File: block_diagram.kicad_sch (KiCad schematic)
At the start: 0 parts

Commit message: Major Changes - Schematic Done??
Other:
- sheet STM32G491RET6 renamed STM32G4
- removed sheet Duplicate Sensors
- sheet Analog ports: added I2S2_CK, I2S2_SD, I2S2_WS, LEFT_SD_MODE, RIGHT_SD_MODE; removed DAC_LEFT_SD_MODE, DAC_RIGHT_SD_MODE, I2S3_CK, I2S3_SD, I2S3_WS
- sheet ESP32C3 ports: added SPI1_MISO, SPI1_MOSI, SPI1_SCLK, SPI_CS_ESP; removed none
- sheet Peripherials ports: added none; removed VBUS_ESP
- sheet Power ports: added 5V_VOLTS, I2C3_SCL, I2C3_SDA, MATRIX_PWR_EN; removed none
- sheet STM32G4 ports: added 5V_VOLTS, ALS_ADC, I2S2_CK, I2S2_SD, I2S2_WS, INT_TEMP_ALERT, LEFT_SD_MODE, MATRIX_PWR_EN, MIC, RIGHT_SD_MODE, SPI1_MISO, SPI1_MOSI, SPI1_SCLK, SPI_CS_ESP, STM32_USB_D_N, STM32_USB_D_P, TV_IR_PWM_1, TV_IR_PWM_2; removed ADC1_IN3, MIC_ADC, PA_3, PC_7
- sheet Sensors ports: added ALS_ADC, I2S3_CK, I2S3_SD, I2S3_WS, INT_TEMP_ALERT, TV_IR_PWM_1, TV_IR_PWM_2; removed LightSense, PA_3, PC_7

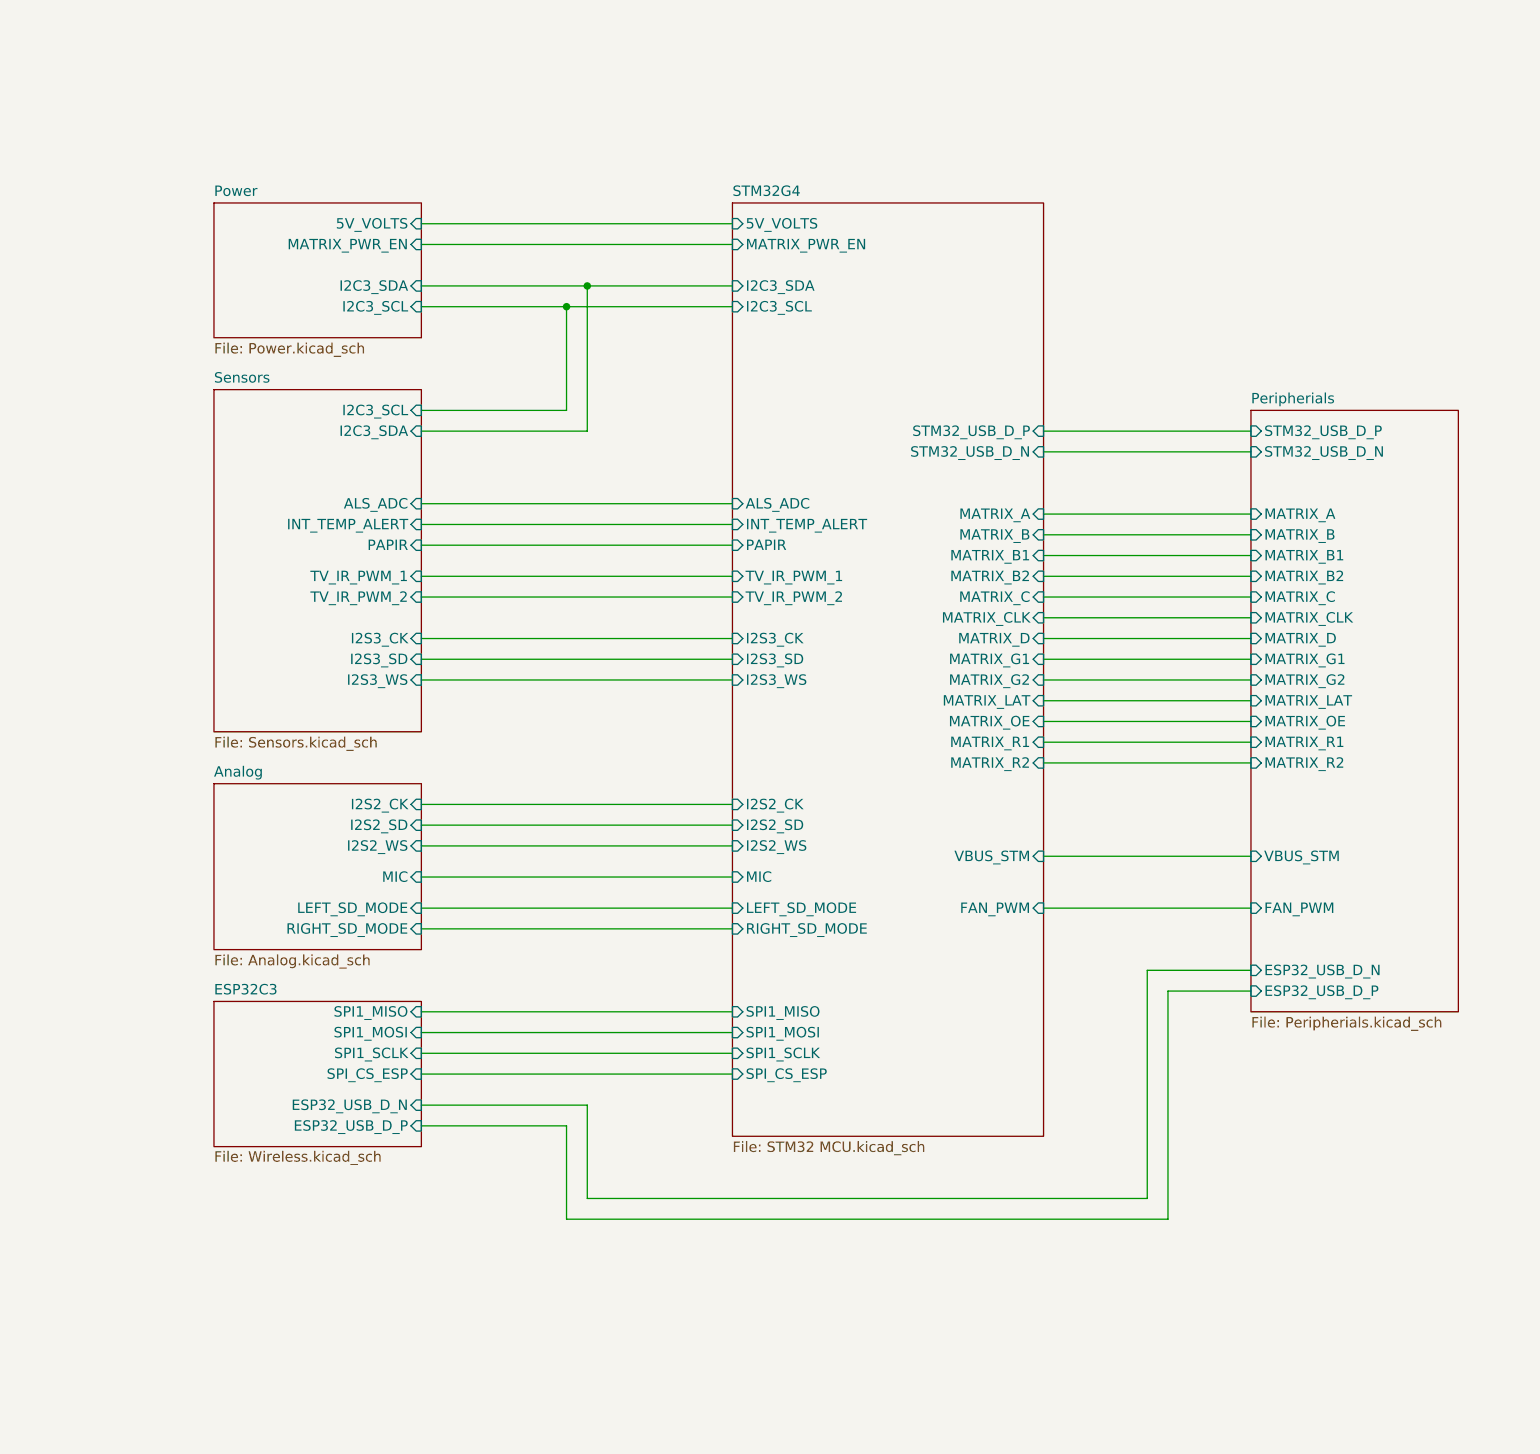
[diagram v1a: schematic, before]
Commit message: PCB Start, Schematic polish
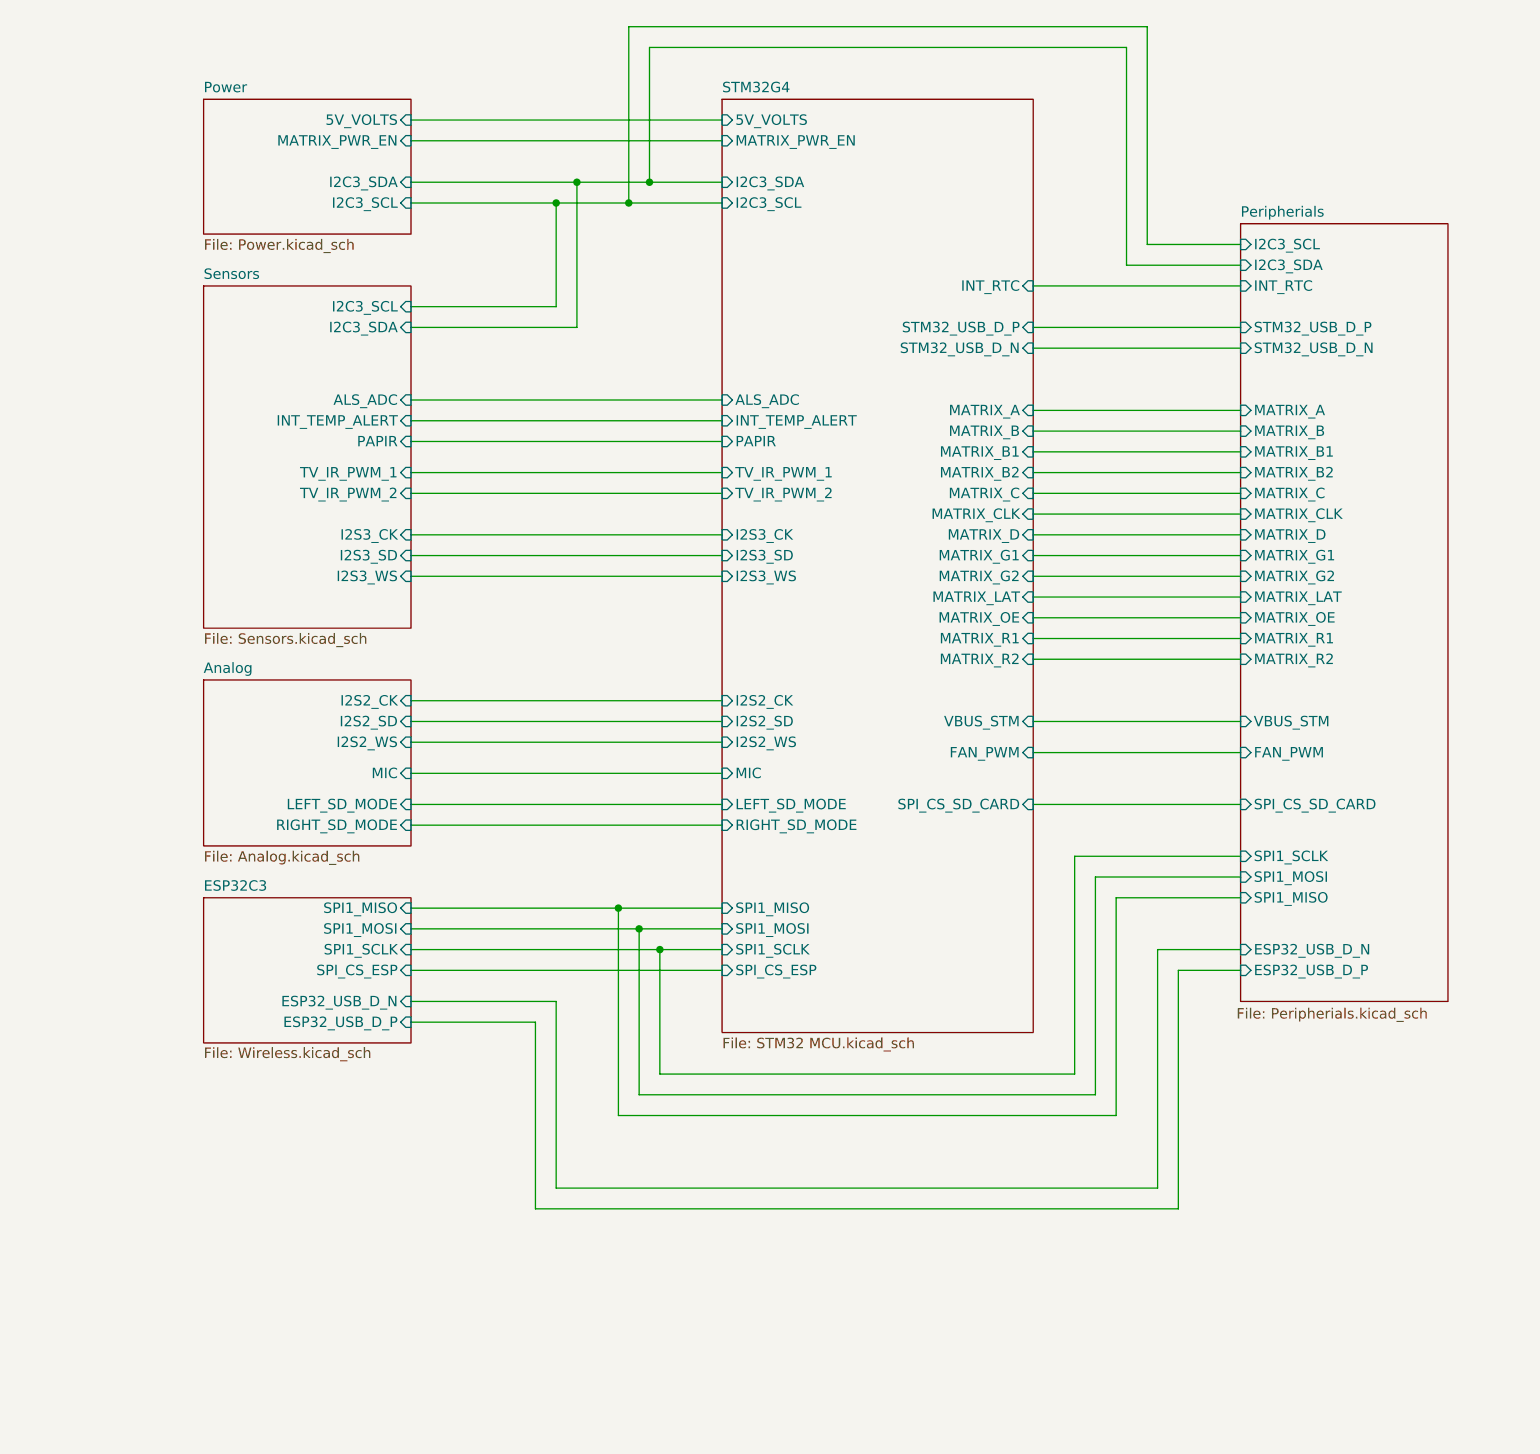
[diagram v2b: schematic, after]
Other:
- sheet Peripherials ports: added I2C3_SCL, I2C3_SDA, INT_RTC, SPI1_MISO, SPI1_MOSI, SPI1_SCLK, SPI_CS_SD_CARD; removed none
- sheet STM32G4 ports: added INT_RTC, SPI_CS_SD_CARD; removed none

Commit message: Minor PCB Changes
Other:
- sheet Peripherials ports: added USB-C_CC1, USB-C_CC2; removed none
- sheet STM32G4 ports: added USB-C_CC1, USB-C_CC2; removed none
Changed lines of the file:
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@@
+	(wire
+		(pts
+			(xy 163.83 40.64) (xy 189.23 40.64)
+		)
+		(stroke
+			(width 0)
+			(type default)
+		)
+	)
 	(wire
 		(pts
@@
 	(wire
 		(pts
-			(xy 177.8 43.18) (xy 177.8 16.51)
+			(xy 177.8 33.02) (xy 177.8 16.51)
 		)
 		(stroke
@@
 	(wire
 		(pts
-			(xy 189.23 43.18) (xy 177.8 43.18)
+			(xy 189.23 33.02) (xy 177.8 33.02)
 		)
 		(stroke
@@
 	(wire
 		(pts
-			(xy 175.26 45.72) (xy 175.26 19.05)
-		)
-		(stroke
-			(width 0)
-			(type default)
-		)
-	)
-	(wire
-		(pts
-			(xy 189.23 45.72) (xy 175.26 45.72)
+			(xy 175.26 35.56) (xy 175.26 19.05)
+		)
+		(stroke
+			(width 0)
+			(type default)
+		)
+	)
+	(wire
+		(pts
+			(xy 189.23 35.56) (xy 175.26 35.56)
 		)
 		(stroke
@@
 		(pts
 			(xy 163.83 66.04) (xy 189.23 66.04)
+		)
+		(stroke
+			(width 0)
+			(type default)
+		)
+	)
+	(wire
+		(pts
+			(xy 163.83 43.18) (xy 189.23 43.18)
 		)
 		(stroke
@@
 			)
 		)
+		(pin "USB-C_CC1" input
+			(at 163.83 40.64 0)
+			(effects
+				(font
+					(size 1.27 1.27)
+				)
+				(justify right)
+			)
+		)
+		(pin "USB-C_CC2" input
+			(at 163.83 43.18 0)
+			(effects
+				(font
+					(size 1.27 1.27)
+				)
+				(justify right)
+			)
+		)
 		(instances
 			(project "SeniorDesign_PCB"
@@
 	)
 	(sheet
-		(at 189.23 40.64)
-		(size 25.4 95.25)
+		(at 189.23 29.21)
+		(size 25.4 105.41)
 		(exclude_from_sim no)
 		(in_bom yes)
@@
 		)
 		(property "Sheetname" "Peripherials"
-			(at 189.23 39.9284 0)
+			(at 189.23 28.4984 0)
 			(show_name no)
 			(do_not_autoplace no)
@@
 		)
 		(property "Sheetfile" "Peripherials.kicad_sch"
-			(at 188.722 136.652 0)
+			(at 189.484 135.636 0)
 			(show_name no)
 			(do_not_autoplace no)
@@
 		)
 		(pin "I2C3_SCL" input
-			(at 189.23 43.18 180)
+			(at 189.23 33.02 180)
 			(effects
 				(font
@@
 		)
 		(pin "I2C3_SDA" input
-			(at 189.23 45.72 180)
+			(at 189.23 35.56 180)
 			(effects
 				(font
@@
 			(effects
 				(font
+					(size 1.27 1.27)
+				)
+				(justify left)
+			)
+		)
+		(pin "USB-C_CC1" input
+			(at 189.23 40.64 180)
+			(effects
+				(font
+					(size 1.27 1.27)
+				)
+				(justify left)
+			)
+		)
+		(pin "USB-C_CC2" input
+			(at 189.23 43.18 180)
+			(effects
+				(font

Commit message: Schematic tiddy up
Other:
- title: (none) -> Block Diagram Schematic
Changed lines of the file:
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@@
 	(generator_version "10.0")
 	(paper "A4")
+	(title_block
+		(title "Block Diagram Schematic")
+		(date "2026-10-17")
+		(rev "0")
+		(comment 1 "Javier Aldana + Xander Beal")
+	)
 	(junction
 		(at 116.84 35.56)

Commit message: Final PCB from Xander
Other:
- sheet Peripherials ports: added none; removed USB-C_CC1, USB-C_CC2
- sheet STM32G4 ports: added none; removed USB-C_CC1, USB-C_CC2
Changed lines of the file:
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@@
-	(wire
-		(pts
-			(xy 163.83 40.64) (xy 189.23 40.64)
-		)
-		(stroke
-			(width 0)
-			(type default)
-		)
-	)
 	(wire
 		(pts
@@
 		(pts
 			(xy 163.83 66.04) (xy 189.23 66.04)
-		)
-		(stroke
-			(width 0)
-			(type default)
-		)
-	)
-	(wire
-		(pts
-			(xy 163.83 43.18) (xy 189.23 43.18)
 		)
 		(stroke
@@
 			)
 		)
-		(pin "USB-C_CC1" input
-			(at 163.83 40.64 0)
-			(effects
-				(font
-					(size 1.27 1.27)
-				)
-				(justify right)
-			)
-		)
-		(pin "USB-C_CC2" input
-			(at 163.83 43.18 0)
-			(effects
-				(font
-					(size 1.27 1.27)
-				)
-				(justify right)
-			)
-		)
 		(instances
 			(project "SeniorDesign_PCB"
@@
 			(effects
 				(font
-					(size 1.27 1.27)
-				)
-				(justify left)
-			)
-		)
-		(pin "USB-C_CC1" input
-			(at 189.23 40.64 180)
-			(effects
-				(font
-					(size 1.27 1.27)
-				)
-				(justify left)
-			)
-		)
-		(pin "USB-C_CC2" input
-			(at 189.23 43.18 180)
-			(effects
-				(font

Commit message: working on power delivery
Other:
- sheet Peripherials ports: added none; removed STM32_USB_D_N, STM32_USB_D_P, VBUS_STM
- sheet Power ports: added STM32_USB_D_N, STM32_USB_D_P, VBUS_STM; removed none
